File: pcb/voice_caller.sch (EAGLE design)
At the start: 53 parts, among them IC1 PRO_MICRO, IC2 LM386M-1, IC3 78L12SMD, K1 TQ2SA-L2-5V, U1 25F32006WSOI

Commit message: Final adjustments.
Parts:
- removed U1: 25F32006WSOI, SparkFun-IC-Memory:SPI_FLASH-X25XXSMD1
- added ARDUINO: PRO_MICRO, SparkFun-Boards:SPARKFUN_PRO_MICRO
- IC1: value PRO_MICRO -> 78L12SMD; device SparkFun-Boards:SPARKFUN_PRO_MICRO -> linear:78L12SMD
- IC3: value 78L12SMD -> 25F32006WSOI; device linear:78L12SMD -> SparkFun-IC-Memory:SPI_FLASH-X25XXSMD1
- renumbered JP1 to SPK, JP2 to LED2, JP3 to LED1, K1 to RLY1
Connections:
- net +3V3: now also ARDUINO.VCC, IC3.HOLD, IC3.VCC, IC3.WP; no longer IC1.VCC, U1.HOLD, U1.VCC, U1.WP
- net +5V: now also ARDUINO.RAW, IC1G$1.VOUT; no longer IC1.RAW, IC3G$1.VOUT
- net +8V: now also IC1G$1.VIN; no longer IC3G$1.VIN
- net BUTTON1: now also ARDUINO.A3, S1.S; no longer IC1.A3, S2.S
- net BUTTON2: now also ARDUINO.A2, S2.S; no longer IC1.A2, S1.S
- net BUTTON3: now also ARDUINO.A0; no longer IC1.A0
- net BUTTON4: now also ARDUINO.*9; no longer IC1.*9
- net BUTTON5: now also ARDUINO.8; no longer IC1.8
- net FLASH_CS: now also ARDUINO.*3, IC3.CS; no longer IC1.*3, U1.CS
- net GND: now also ARDUINO.GND, ARDUINO.GND@1, ARDUINO.GND@2, IC1G$1.GND@1, IC1G$1.GND@2, IC1G$1.GND@3, IC1G$1.GND@4, IC3.GND; no longer IC1.GND, IC1.GND@1, IC1.GND@2, IC3G$1.GND@1, IC3G$1.GND@2, IC3G$1.GND@3, IC3G$1.GND@4, U1.GND
- net MISO: now also ARDUINO.12(MISO), IC3.MISO; no longer IC1.12(MISO), U1.MISO
- net MOSI: now also ARDUINO.11(MOSI), IC3.MOSI; no longer IC1.11(MOSI), U1.MOSI
- net N$12: now also ARDUINO.*6; no longer IC1.*6
- net N$15: now also ARDUINO.7; no longer IC1.7
- net PTT_SENSE: now also ARDUINO.A1; no longer IC1.A1
- net PTT_SW: now also ARDUINO.2; no longer IC1.2
- net PULSE_RX: now also ARDUINO.*5; no longer IC1.*5
- net PULSE_TX: now also ARDUINO.4; no longer IC1.4
- net PWM: now also ARDUINO.*10; no longer IC1.*10
- net SCK: now also ARDUINO.13(SCK), IC3.SCK; no longer IC1.13(SCK), U1.SCK
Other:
- moved on the sheet: S1, S2

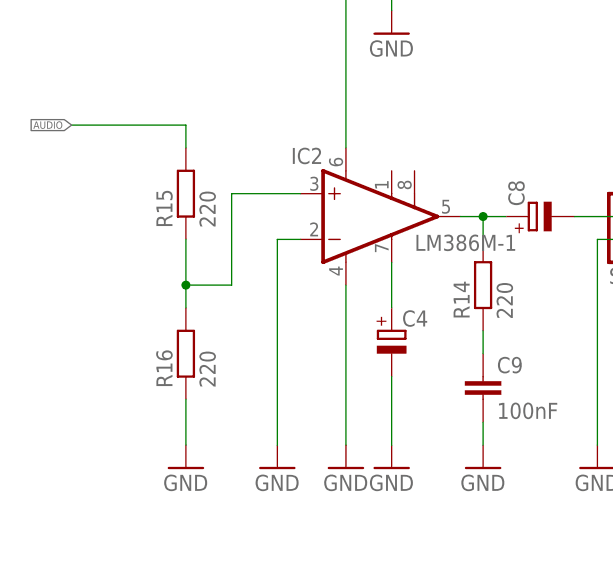
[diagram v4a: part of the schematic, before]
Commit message: AF amp attenuator changed.
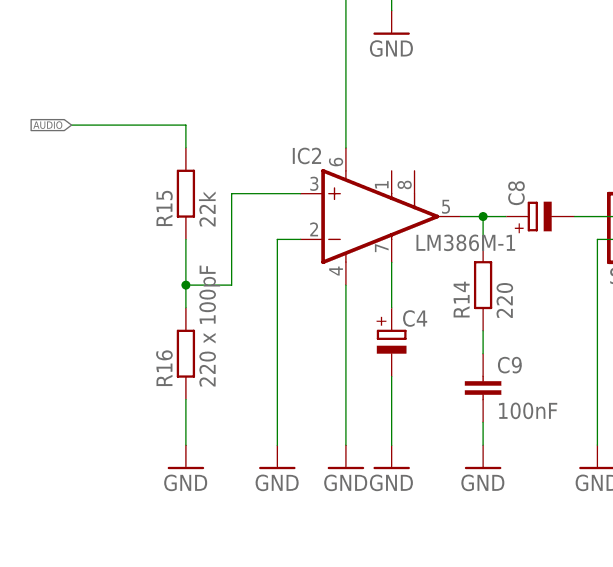
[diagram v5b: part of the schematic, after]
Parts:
- R15: value 220 -> 22k
- R16: value 220 -> 220 x 100pF
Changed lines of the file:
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@@
 <part name="GND24" library="supply1" deviceset="GND" device=""/>
 <part name="GND25" library="supply1" deviceset="GND" device=""/>
-<part name="R15" library="rcl" deviceset="R-EU_" device="M1206" value="220"/>
-<part name="R16" library="rcl" deviceset="R-EU_" device="M1206" value="220"/>
+<part name="R15" library="rcl" deviceset="R-EU_" device="M1206" value="22k"/>
+<part name="R16" library="rcl" deviceset="R-EU_" device="M1206" value="220 x 100pF"/>
 <part name="C11" library="rcl" deviceset="CPOL-EU" device="E2.5-6"/>
 <part name="GND26" library="supply1" deviceset="GND" device=""/>

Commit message: Jumper wire added.
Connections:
- removed net VCC: C10.1, IC2.VS
- net +8V: now also C10.1, IC2.VS
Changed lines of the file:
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@@
 <wire x1="147.32" y1="144.78" x2="147.32" y2="147.32" width="0.1524" layer="91"/>
+</segment>
+<segment>
+<pinref part="IC2" gate="G$1" pin="VS"/>
+<wire x1="-73.66" y1="127" x2="-73.66" y2="154.94" width="0.1524" layer="91"/>
+<pinref part="+8V1" gate="VCC" pin="VCC"/>
+<pinref part="C10" gate="G$1" pin="1"/>
+<wire x1="-73.66" y1="154.94" x2="-73.66" y2="157.48" width="0.1524" layer="91"/>
+<wire x1="-68.58" y1="152.4" x2="-68.58" y2="154.94" width="0.1524" layer="91"/>
+<wire x1="-68.58" y1="154.94" x2="-73.66" y2="154.94" width="0.1524" layer="91"/>
+<junction x="-73.66" y="154.94"/>
 </segment>
 </net>
@@
 </segment>
 </net>
-<net name="VCC" class="0">
-<segment>
-<pinref part="IC2" gate="G$1" pin="VS"/>
-<wire x1="-73.66" y1="127" x2="-73.66" y2="154.94" width="0.1524" layer="91"/>
-<pinref part="+8V1" gate="VCC" pin="VCC"/>
-<pinref part="C10" gate="G$1" pin="1"/>
-<wire x1="-73.66" y1="154.94" x2="-73.66" y2="157.48" width="0.1524" layer="91"/>
-<wire x1="-68.58" y1="152.4" x2="-68.58" y2="154.94" width="0.1524" layer="91"/>
-<wire x1="-68.58" y1="154.94" x2="-73.66" y2="154.94" width="0.1524" layer="91"/>
-<junction x="-73.66" y="154.94"/>
-</segment>
-</net>
